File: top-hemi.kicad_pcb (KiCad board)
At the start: 2 copper layers, 46 x 39 mm, 37 parts, among them J1 USB_B_Mini, J2 TC2030_NL, J3 FFC-0.5MM-6POS, J4 Port_1, J5 Port_2, J6 FFC-0.5MM-6POS, J7 Port_3, J8 Port_4, U1 PMIC-LDO-XC6204B332MR_SOT23-5_, U2 LP2985-5.0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

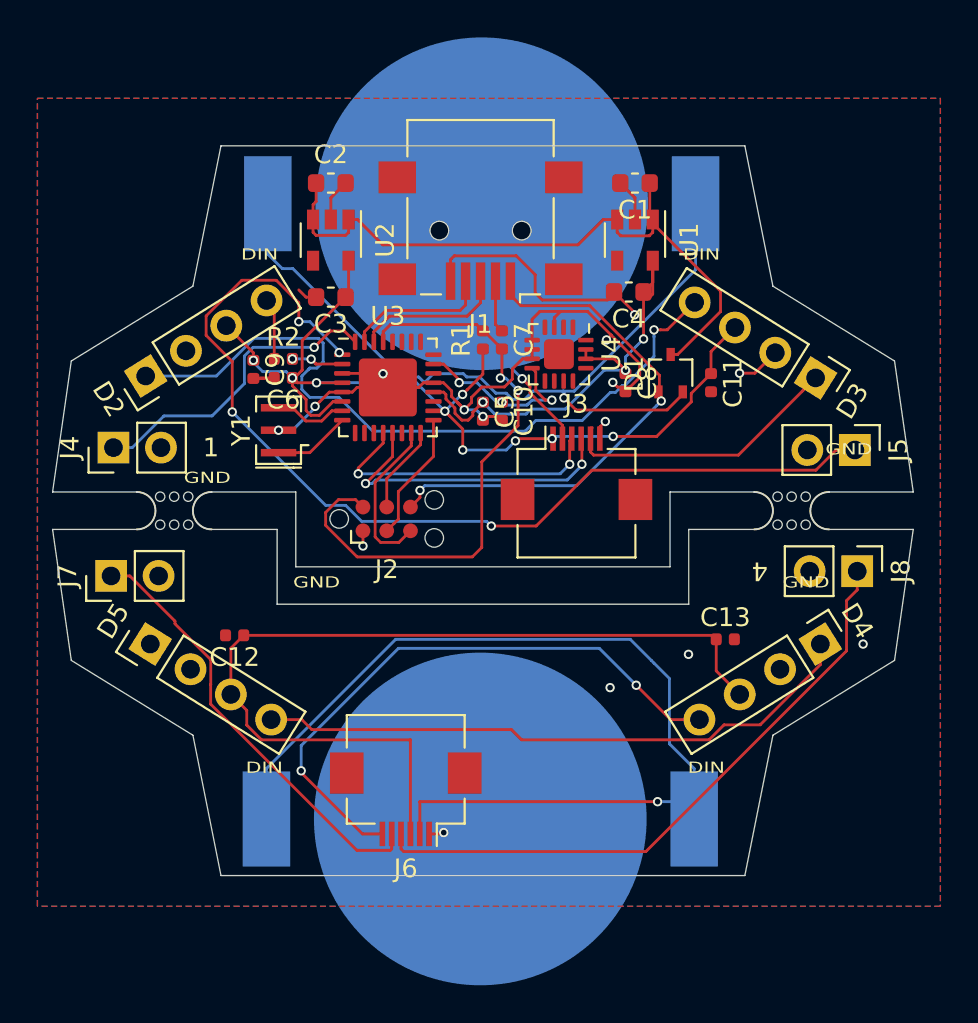
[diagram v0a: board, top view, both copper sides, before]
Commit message: Swap LEDs 3 and 4
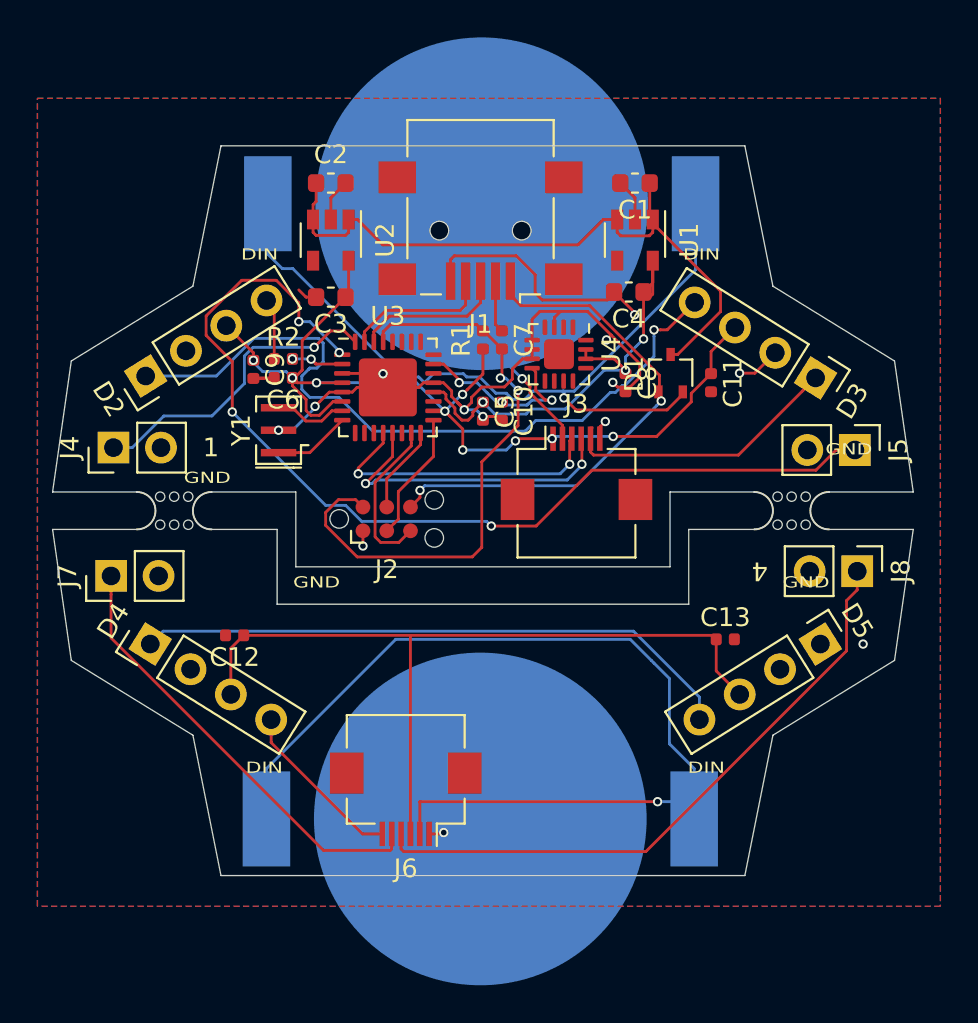
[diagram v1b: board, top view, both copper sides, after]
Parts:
- moved D4 35.8 mm to (129.2, 90.1), turned to 58 degrees
- moved D5 35.8 mm to (165.0, 90.1), turned to 302 degrees
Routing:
- net /Bottom hemisphere/DIN-BOT: track 32.2 -> 9.19 mm, vias 2 -> 0
- net +5V: track 101.7 -> 96.2 mm
- net GND: vias 15 -> 13

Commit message: Connect USB-Mini shield to GND
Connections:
- J1 pad 6: Net-(J1-Pad6) -> GND
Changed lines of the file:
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@@
     (zones 0)
     (modules 37)
-    (nets 49)
+    (nets 48)
   )
   (page A4)
   (layers
-    (0 F.Cu signal)
+    (0 F.Cu signal hide)
     (31 B.Cu signal)
     (32 B.Adhes user hide)
@@
   (net 45 "Net-(U4-Pad10)")
   (net 46 "Net-(U4-Pad12)")
-  (net 47 "Net-(J1-Pad6)")
-  (net 48 "Net-(D5-Pad1)")
+  (net 47 "Net-(D5-Pad1)")
   (net_class Default "This is the default net class."
     (clearance 0.1524)
@@
     (add_net "Net-(D4-Pad1)")
     (add_net "Net-(D5-Pad1)")
-    (add_net "Net-(J1-Pad6)")
     (add_net "Net-(R2-Pad2)")
     (add_net "Net-(U1-Pad4)")
@@
       (net 3 GND))
     (pad 6 smd rect (at -4.45 -2.6 180) (size 2 1.7) (layers F.Cu F.Paste F.Mask)
-      (net 47 "Net-(J1-Pad6)"))
+      (net 3 GND))
     (pad 6 smd rect (at -4.45 2.85 180) (size 2 1.7) (layers F.Cu F.Paste F.Mask)
-      (net 47 "Net-(J1-Pad6)"))
+      (net 3 GND))
     (pad 6 smd rect (at 4.45 -2.6 180) (size 2 1.7) (layers F.Cu F.Paste F.Mask)
-      (net 47 "Net-(J1-Pad6)"))
+      (net 3 GND))
     (pad 6 smd rect (at 4.45 2.85 180) (size 2 1.7) (layers F.Cu F.Paste F.Mask)
-      (net 47 "Net-(J1-Pad6)"))
+      (net 3 GND))
     (pad "" np_thru_hole circle (at -2.2 0 180) (size 1 1) (drill 1) (layers *.Cu *.Mask))
     (pad "" np_thru_hole circle (at 2.2 0 180) (size 1 1) (drill 1) (layers *.Cu *.Mask))
@@
       (net 3 GND))
     (pad 1 thru_hole rect (at 0 0 302) (size 1.7 1.7) (drill 1) (layers *.Cu *.Mask)
-      (net 48 "Net-(D5-Pad1)"))
+      (net 47 "Net-(D5-Pad1)"))
     (model ${KISYS3DMOD}/Connector_PinHeader_2.54mm.3dshapes/PinHeader_1x04_P2.54mm_Vertical.wrl
       (at (xyz 0 0 0))
@@
   (segment (start 128.975916 75.80199) (end 132.752211 75.80199) (width 0.1524) (layer B.Cu) (net 12))
   (segment (start 138.461986 74.039383) (end 138.461986 75.044014) (width 0.1524) (layer B.Cu) (net 12))
-  (segment (start 138.461986 75.044014) (end 138.127412 75.378588) (width 0.1524) (layer B.Cu) (net 12))
-  (segment (start 137.750012 75.378588) (end 137.6673 75.4613) (width 0.1524) (layer B.Cu) (net 12))
-  (segment (start 138.127412 75.378588) (end 137.750012 75.378588) (width 0.1524) (layer B.Cu) (net 12))
-  (segment (start 137.750014 75.378587) (end 137.6673 75.4613) (width 0.1524) (layer B.Cu) (net 12))
   (segment (start 158.317874 71.866015) (end 156.849279 73.33461) (width 0.1524) (layer F.Cu) (net 12))
   (segment (start 156.849279 73.33461) (end 156.497553 73.33461) (width 0.1524) (layer F.Cu) (net 12))
@@
   (segment (start 156.144 74.752998) (end 156.144 73.688163) (width 0.1524) (layer B.Cu) (net 12))
   (segment (start 154.453019 76.310378) (end 154.58662 76.310378) (width 0.1524) (layer B.Cu) (net 12))
-  (segment (start 137.322587 76.517986) (end 137.750014 76.945413) (width 0.1524) (layer B.Cu) (net 12))
-  (segment (start 137.750014 76.945413) (end 139.305279 76.945413) (width 0.1524) (layer B.Cu) (net 12))
   (segment (start 152.308456 78.177288) (end 153.808391 76.677353) (width 0.1524) (layer B.Cu) (net 12))
   (segment (start 141.108677 78.748811) (end 149.256748 78.748811) (width 0.1524) (layer B.Cu) (net 12))
   (segment (start 156.144 73.688163) (end 156.144 73.33461) (width 0.1524) (layer B.Cu) (net 12))
-  (segment (start 137.322587 75.806014) (end 137.322587 76.517986) (width 0.1524) (layer B.Cu) (net 12))
   (segment (start 139.305279 76.945413) (end 141.108677 78.748811) (width 0.1524) (layer B.Cu) (net 12))
-  (segment (start 137.6673 75.4613) (end 137.322587 75.806014) (width 0.1524) (layer B.Cu) (net 12))
   (segment (start 154.086045 76.677353) (end 154.453019 76.310378) (width 0.1524) (layer B.Cu) (net 12))
   (segment (start 149.828271 78.177288) (end 152.308456 78.177288) (width 0.1524) (layer B.Cu) (net 12))
   (segment (start 153.808391 76.677353) (end 154.086045 76.677353) (width 0.1524) (layer B.Cu) (net 12))
   (segment (start 154.58662 76.310378) (end 156.144 74.752998) (width 0.1524) (layer B.Cu) (net 12))
+  (segment (start 137.750014 76.945413) (end 139.305279 76.945413) (width 0.1524) (layer B.Cu) (net 12))
+  (segment (start 137.750014 75.378587) (end 137.6673 75.4613) (width 0.1524) (layer B.Cu) (net 12))
+  (segment (start 137.750012 75.378588) (end 137.6673 75.4613) (width 0.1524) (layer B.Cu) (net 12))
+  (segment (start 137.322587 76.517986) (end 137.750014 76.945413) (width 0.1524) (layer B.Cu) (net 12))
+  (segment (start 137.322587 75.806014) (end 137.322587 76.517986) (width 0.1524) (layer B.Cu) (net 12))
+  (segment (start 137.6673 75.4613) (end 137.322587 75.806014) (width 0.1524) (layer B.Cu) (net 12))
+  (segment (start 138.127412 75.378588) (end 137.750012 75.378588) (width 0.1524) (layer B.Cu) (net 12))
+  (segment (start 138.461986 75.044014) (end 138.127412 75.378588) (width 0.1524) (layer B.Cu) (net 12))
   (segment (start 135.847 72.172963) (end 135.438042 71.764005) (width 0.1524) (layer F.Cu) (net 13) (status 30))
   (segment (start 135.847 74.888) (end 135.847 72.172963) (width 0.1524) (layer F.Cu) (net 13) (status 30))
